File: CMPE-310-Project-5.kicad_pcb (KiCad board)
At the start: 2 copper layers, 6 parts, among them J1 DSUB-9, U1 max235cpg, U2 28F010, U3 pkd8279, U4 8086_Min_Mode

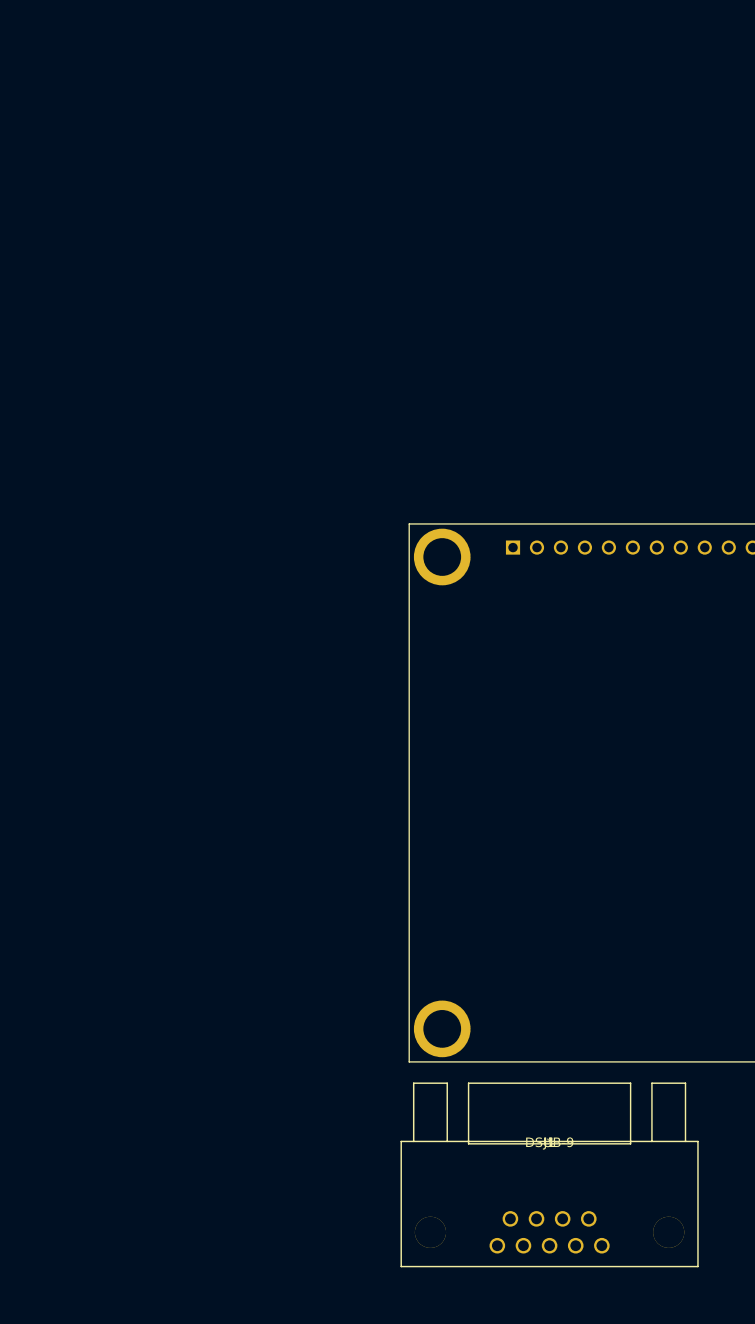
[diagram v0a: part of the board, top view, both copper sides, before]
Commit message: DSUB-9 moved
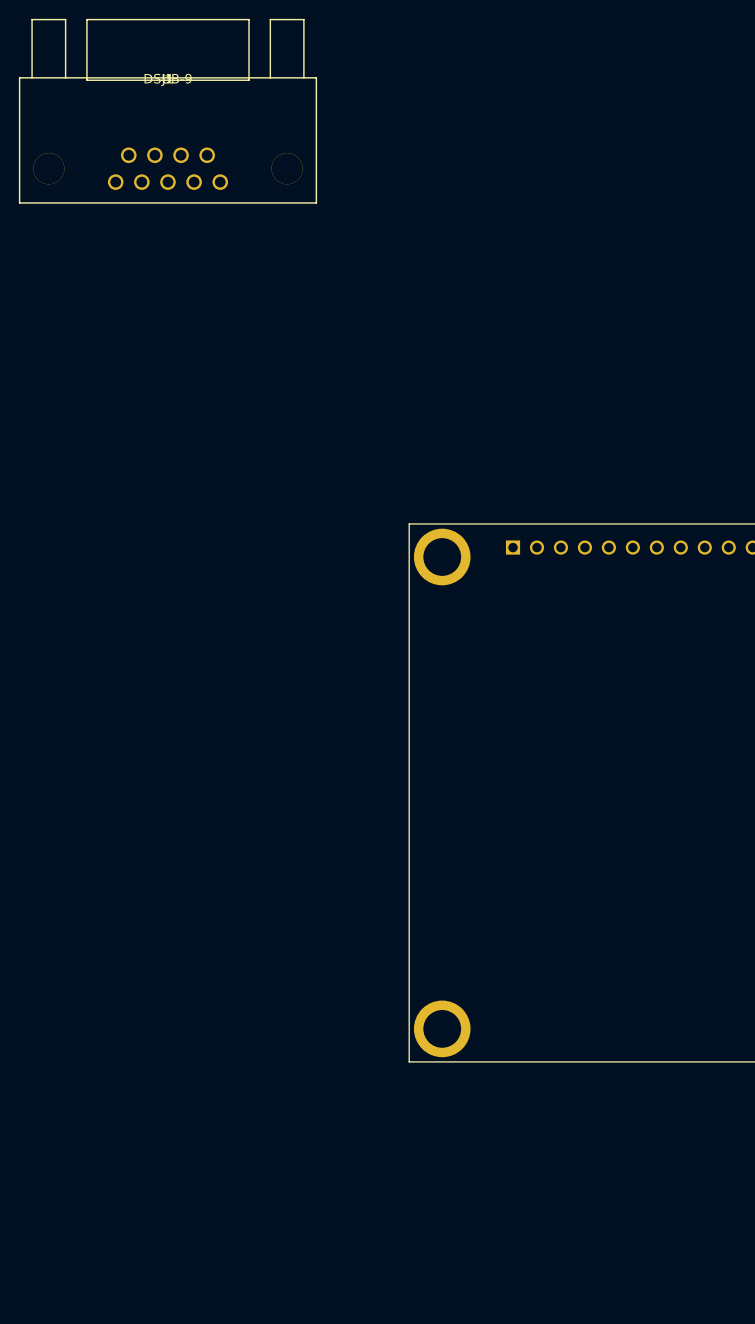
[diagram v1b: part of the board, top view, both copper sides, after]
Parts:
- moved J1 119.7 mm to (50.8, -1.38)
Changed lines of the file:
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@@
   )
   (footprint "parts:DSUB-9" (layer "F.Cu")
-    (at 91.2358 111.3124)
+    (at 50.8 -1.3843)
     (descr "DSUB-9-2")
     (tags "UART")

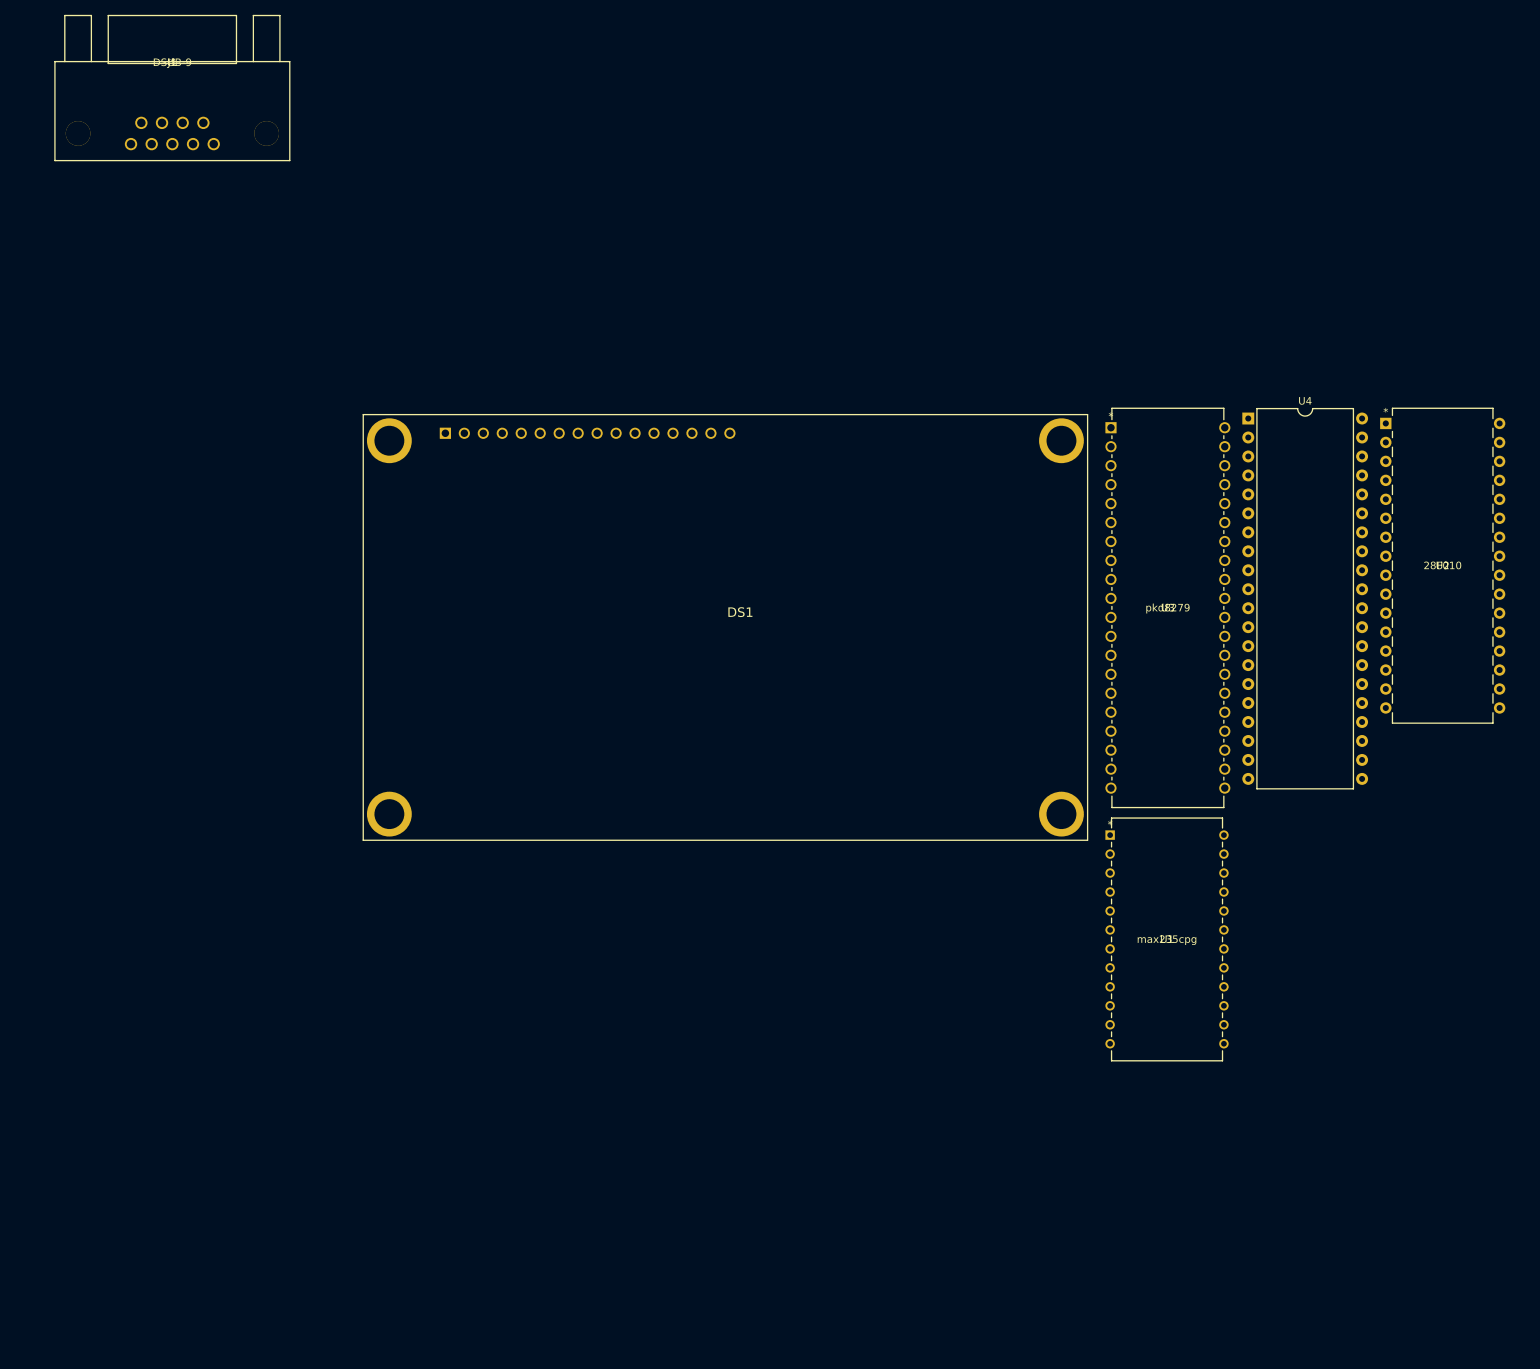
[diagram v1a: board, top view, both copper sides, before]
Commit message: Create CMPE-310-Project-5-2022-04-23_144547.zip
Added Wiring for the 28F010 (CMOS)
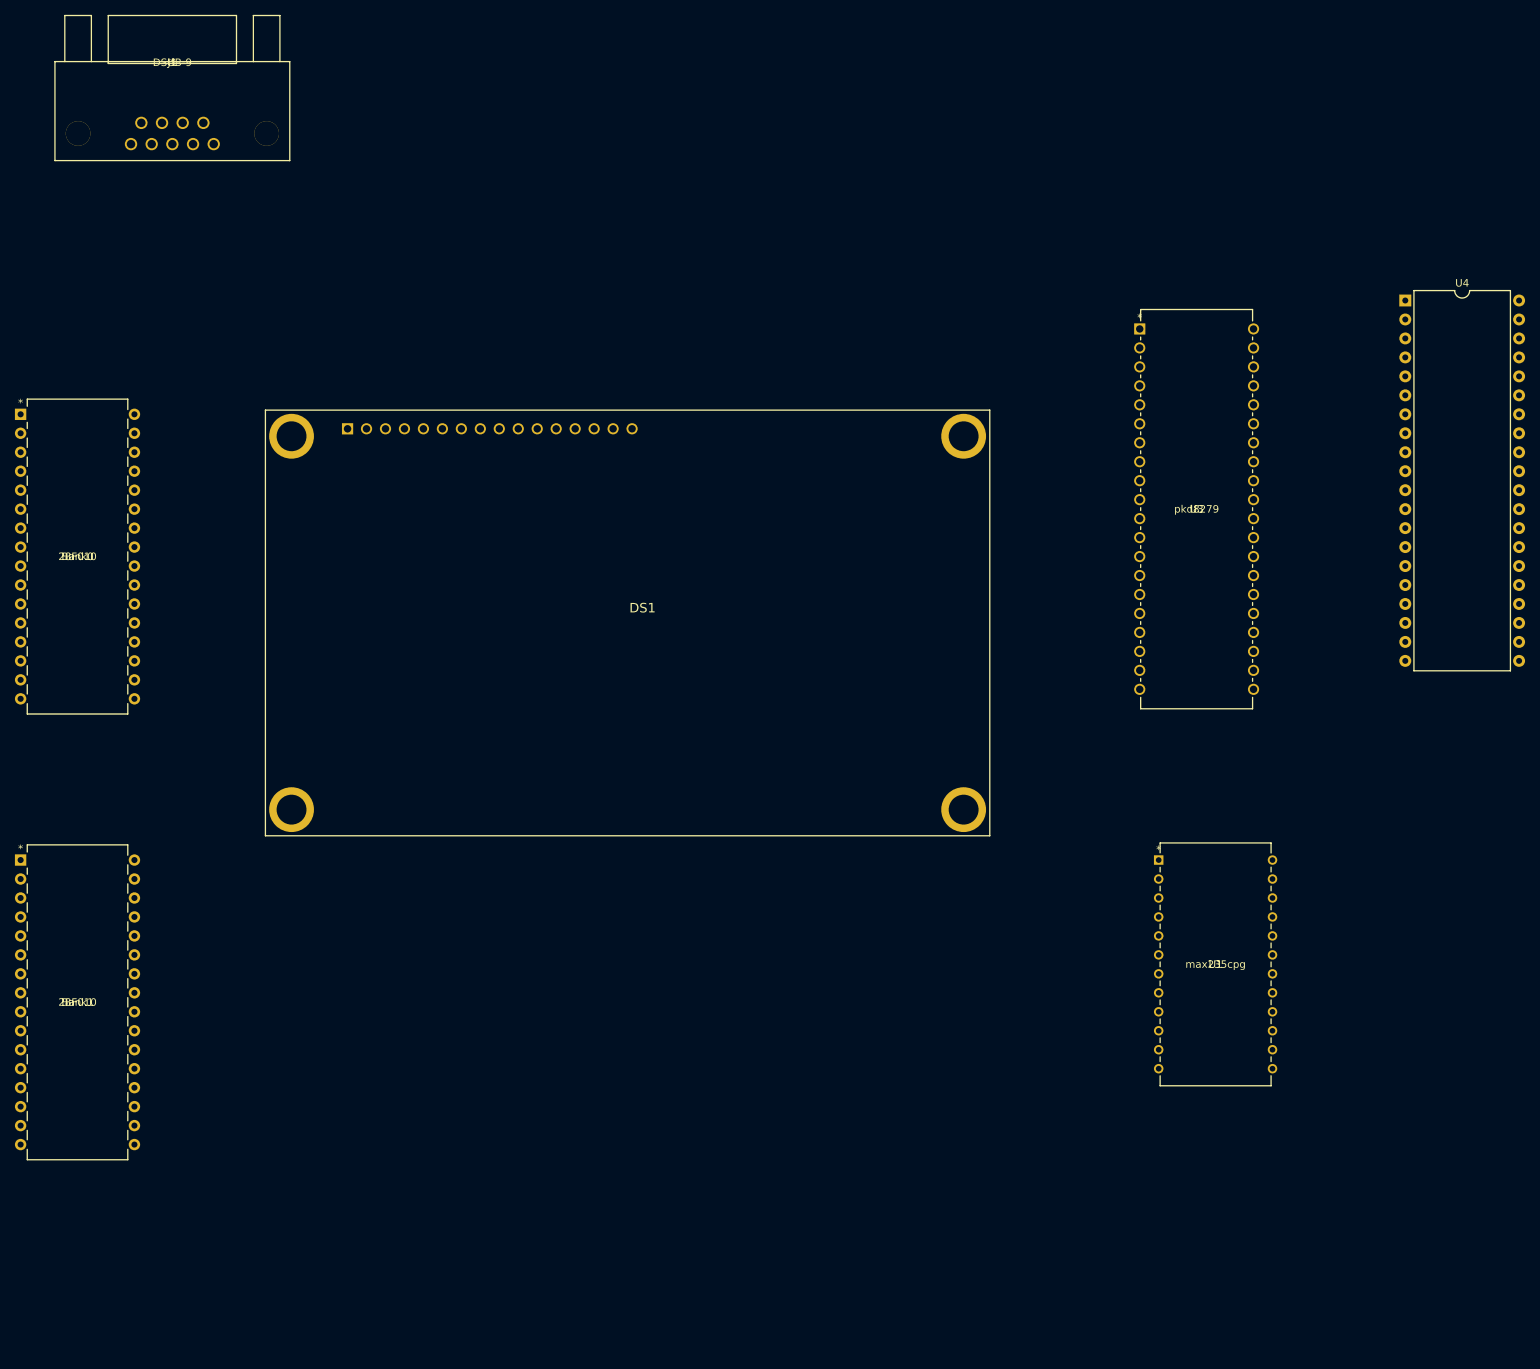
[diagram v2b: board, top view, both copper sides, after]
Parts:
- removed U2: 28F010, parts:28F010
- added Bank0: 28F010, parts:28F010, F.Cu at (30.5, 45.7)
- added Bank1: 28F010, parts:28F010, F.Cu at (30.5, 105.4)
- moved U4 26.3 mm to (215.9, 30.5)
- moved U3 13.8 mm to (195.6, 82.5)
- moved DS1 13.1 mm to (73.3, 47.7)
- moved U1 7.31 mm to (198.1, 133.3)
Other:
- copper layers 2 -> 4

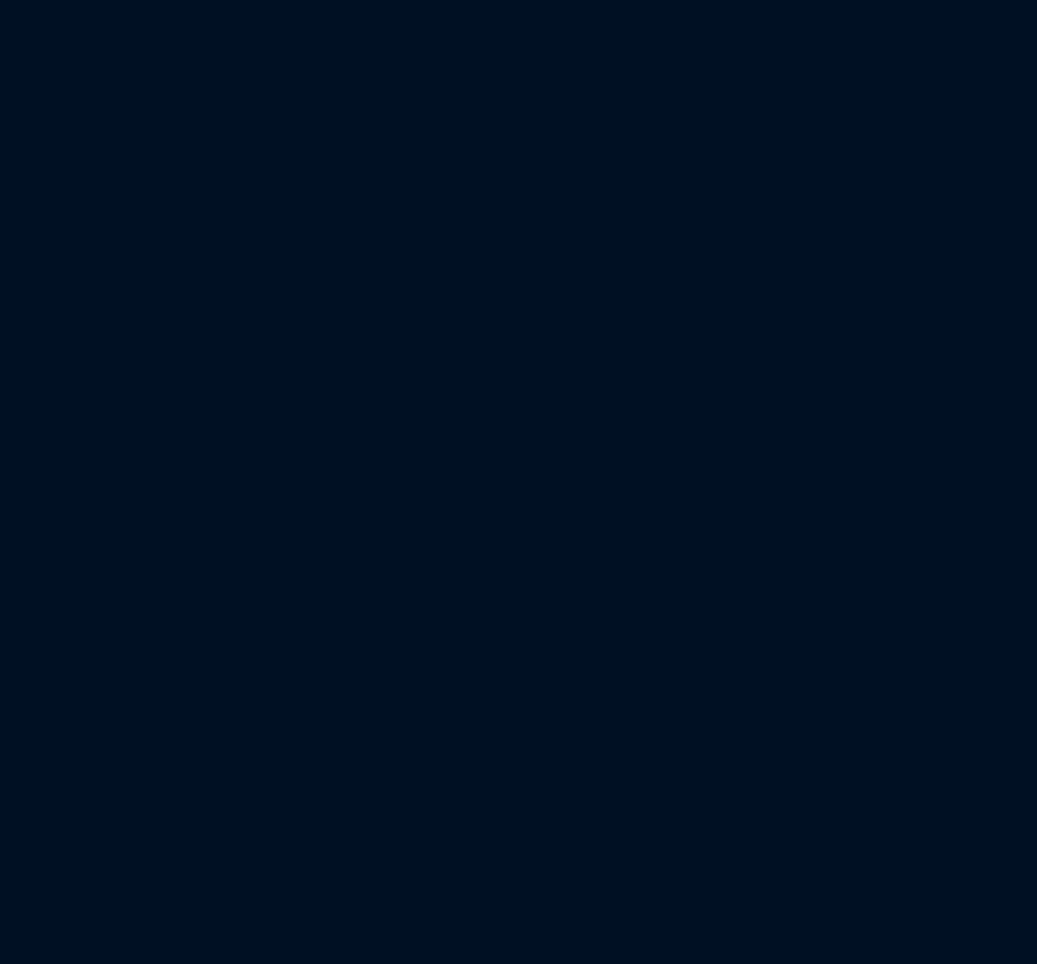
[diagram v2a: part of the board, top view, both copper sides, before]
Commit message: Updated PCB
Updated PCB with 8255 sheet
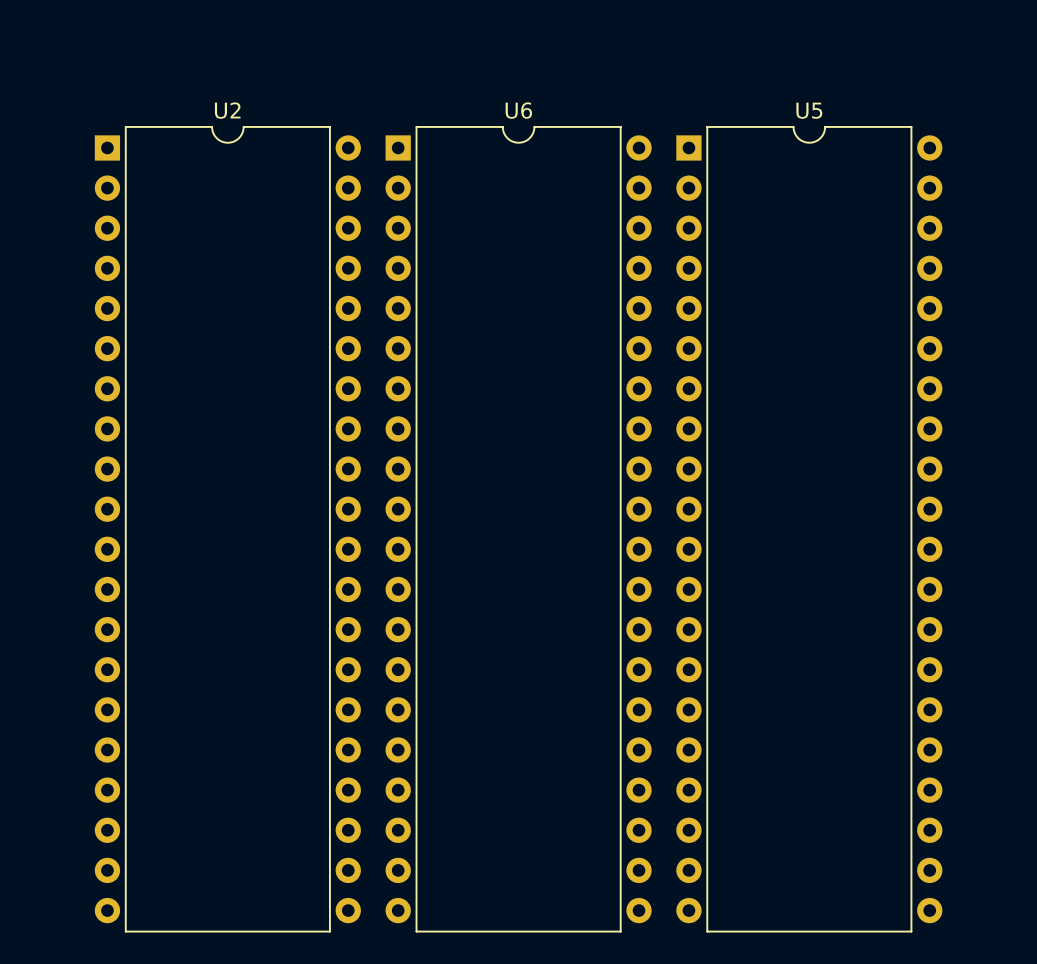
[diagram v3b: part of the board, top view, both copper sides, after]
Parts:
- added U2: 8255, Package_DIP:DIP-40_W15.24mm, F.Cu at (78.7, 121.9)
- added U5: 8255, Package_DIP:DIP-40_W15.24mm, F.Cu at (115.5, 121.9)
- added U6: 8255, Package_DIP:DIP-40_W15.24mm, F.Cu at (97.1, 121.9)
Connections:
- U4 pad 10: unconnected-(U4-Pad10) -> /A6
- U4 pad 11: unconnected-(U4-Pad11) -> /A5
- U4 pad 12: unconnected-(U4-Pad12) -> /A4
- U4 pad 13: unconnected-(U4-Pad13) -> /A3
- U4 pad 14: unconnected-(U4-Pad14) -> /A2
- U4 pad 15: unconnected-(U4-Pad15) -> /A1
- U4 pad 16: unconnected-(U4-Pad16) -> /A0
- U4 pad 2: unconnected-(U4-Pad2) -> /A14
- U4 pad 28: unconnected-(U4-Pad28) -> /M/IO
- U4 pad 29: unconnected-(U4-Pad29) -> /WR
- U4 pad 3: unconnected-(U4-Pad3) -> /A13
- U4 pad 32: unconnected-(U4-Pad32) -> /RD
- U4 pad 35: unconnected-(U4-Pad35) -> /A19
- U4 pad 36: unconnected-(U4-Pad36) -> /A18
- U4 pad 37: unconnected-(U4-Pad37) -> /A17
- U4 pad 38: unconnected-(U4-Pad38) -> /A16
- U4 pad 39: unconnected-(U4-Pad39) -> /A15
- U4 pad 4: unconnected-(U4-Pad4) -> /A12
- U4 pad 5: unconnected-(U4-Pad5) -> /A11
- U4 pad 6: unconnected-(U4-Pad6) -> /A10
- U4 pad 7: unconnected-(U4-Pad7) -> /A9
- U4 pad 8: unconnected-(U4-Pad8) -> /A8
- U4 pad 9: unconnected-(U4-Pad9) -> /A7
